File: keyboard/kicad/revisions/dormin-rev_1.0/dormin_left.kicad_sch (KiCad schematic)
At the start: 104 parts, among them J2 Conn_01x04, Q1 AO3400A, Q2 AO3407A, SW1 SW_Push, SW10 SW_Push, SW11 SW_Push, SW12 SW_Push, SW13 SW_Push, SW14 SW_Push, SW15 SW_Push, SW16 SW_Push, SW17 SW_Push, SW18 SW_Push, SW19 SW_Push, SW2 SW_Push, SW20 SW_Push, SW3 SW_Push, SW4 SW_Push, SW5 SW_Push, SW6 SW_Push, SW7 SW_Push, SW8 SW_Push, SW9 SW_Push, U1 Seeeduino Xiao nRF52840

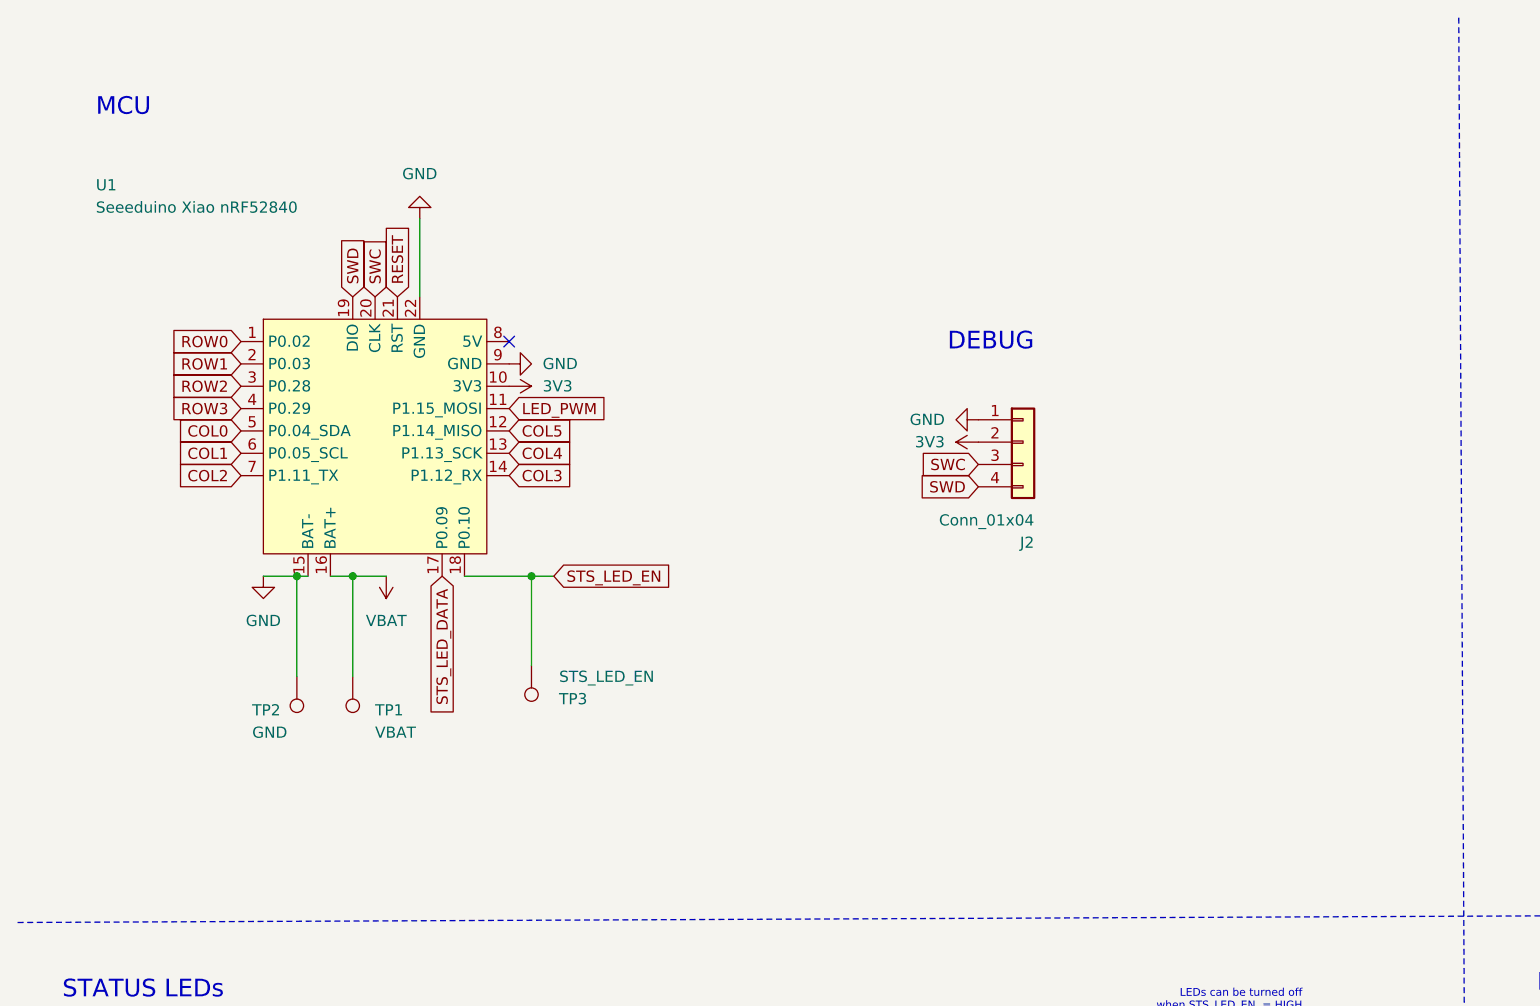
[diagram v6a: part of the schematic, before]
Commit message: refactor: fix xiao footprint and symbol
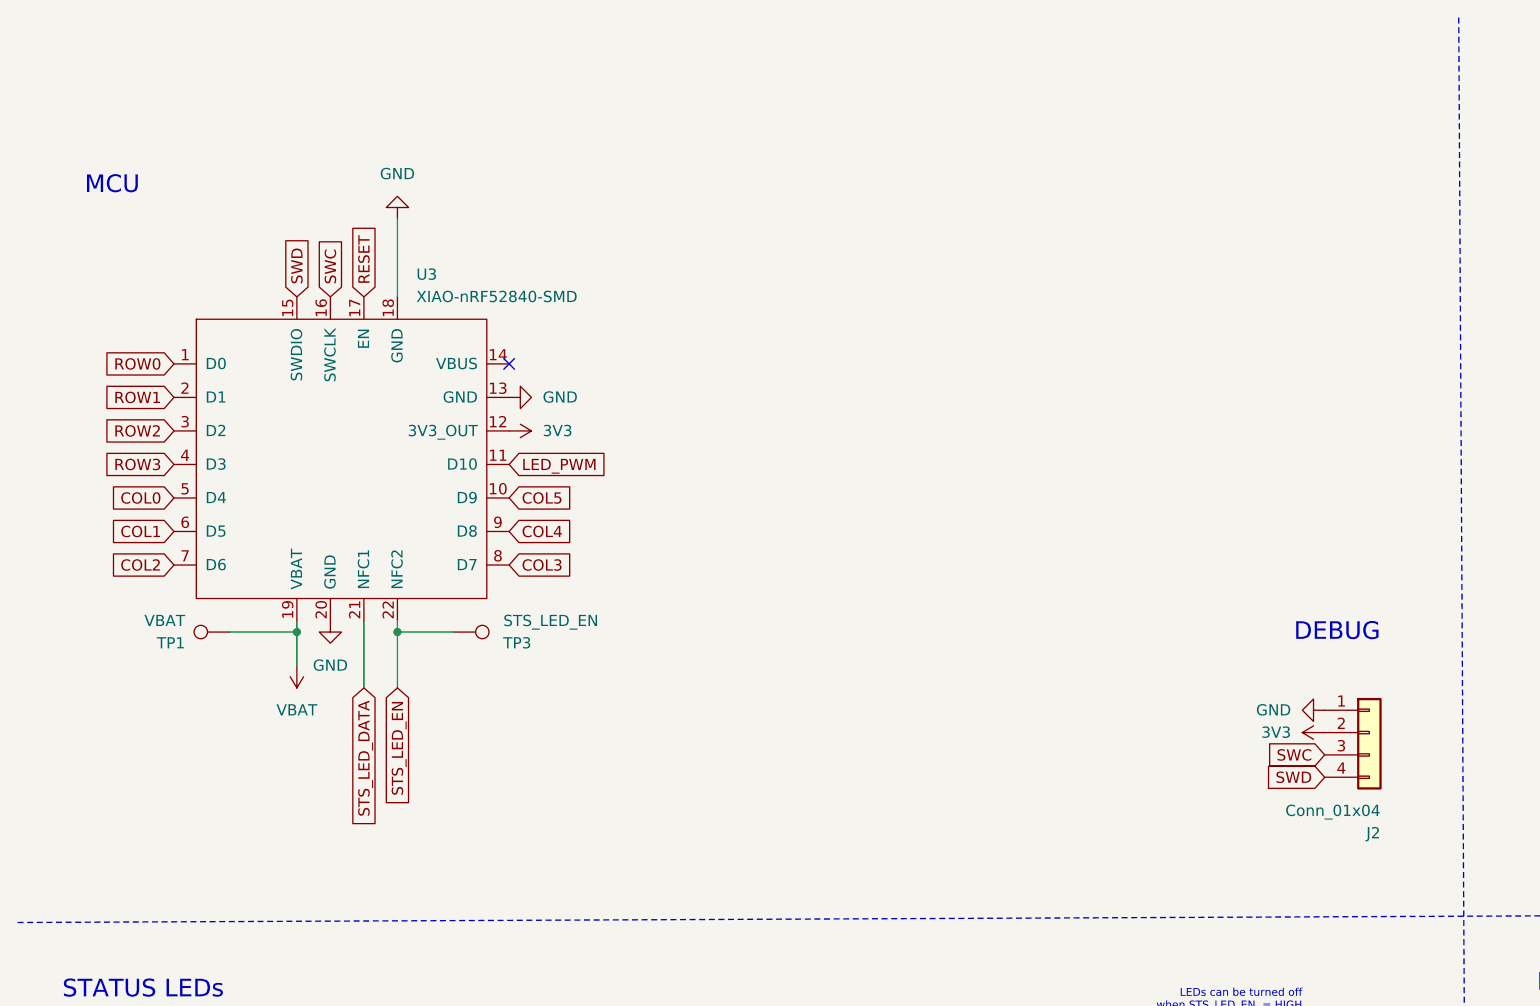
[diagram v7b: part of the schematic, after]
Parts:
- removed TP2: GND, TestPoint:TestPoint_Pad_D1.0mm, symbol Connector:TestPoint
- removed U1: Seeeduino Xiao nRF52840, Seeed_Studio_XIAO_Series:XIAO-nRF52840-SMD, symbol PCM_marbastlib-promicroish:Seeeduino_Xiao_nRF52840
- added U3: XIAO-nRF52840-SMD, Seeed_Studio_XIAO_Series:XIAO-nRF52840-SMD, symbol Seeed_Studio_XIAO_Series:XIAO-nRF52840-SMD
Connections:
- net 3V3: now also U3.12 (3V3_OUT)
- net COL0: now also U3.5 (D4)
- net COL1: now also U3.6 (D5)
- net COL2: now also U3.7 (D6)
- net COL3: now also U3.8 (D7)
- net COL4: now also U3.9 (D8)
- net COL5: now also U3.10 (D9)
- net GND: now also U3.13 (GND), U3.18 (GND), U3.20 (GND)
- net LED_PWM: now also U3.11 (D10)
- net RESET: now also U3.17 (EN)
- net ROW0: now also U3.1 (D0)
- net ROW1: now also U3.2 (D1)
- net ROW2: now also U3.3 (D2)
- net ROW3: now also U3.4 (D3)
- net STS_LED_DATA: now also U3.21 (NFC1)
- net STS_LED_EN: now also U3.22 (NFC2)
- net SWC: now also U3.16 (SWCLK)
- net SWD: now also U3.15 (SWDIO)
- net VBAT: now also U3.19 (VBAT)
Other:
- moved on the sheet: J2, TP3
